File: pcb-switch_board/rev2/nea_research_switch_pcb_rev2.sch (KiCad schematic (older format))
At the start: 20 parts, among them P1 CONN_02X15, P2 CONN_02X13, P3 CONN_02X30, U1 QS4A110, U2 QS4A110, U3 QS4A110, U4 QS4A110, U5 QS4A110

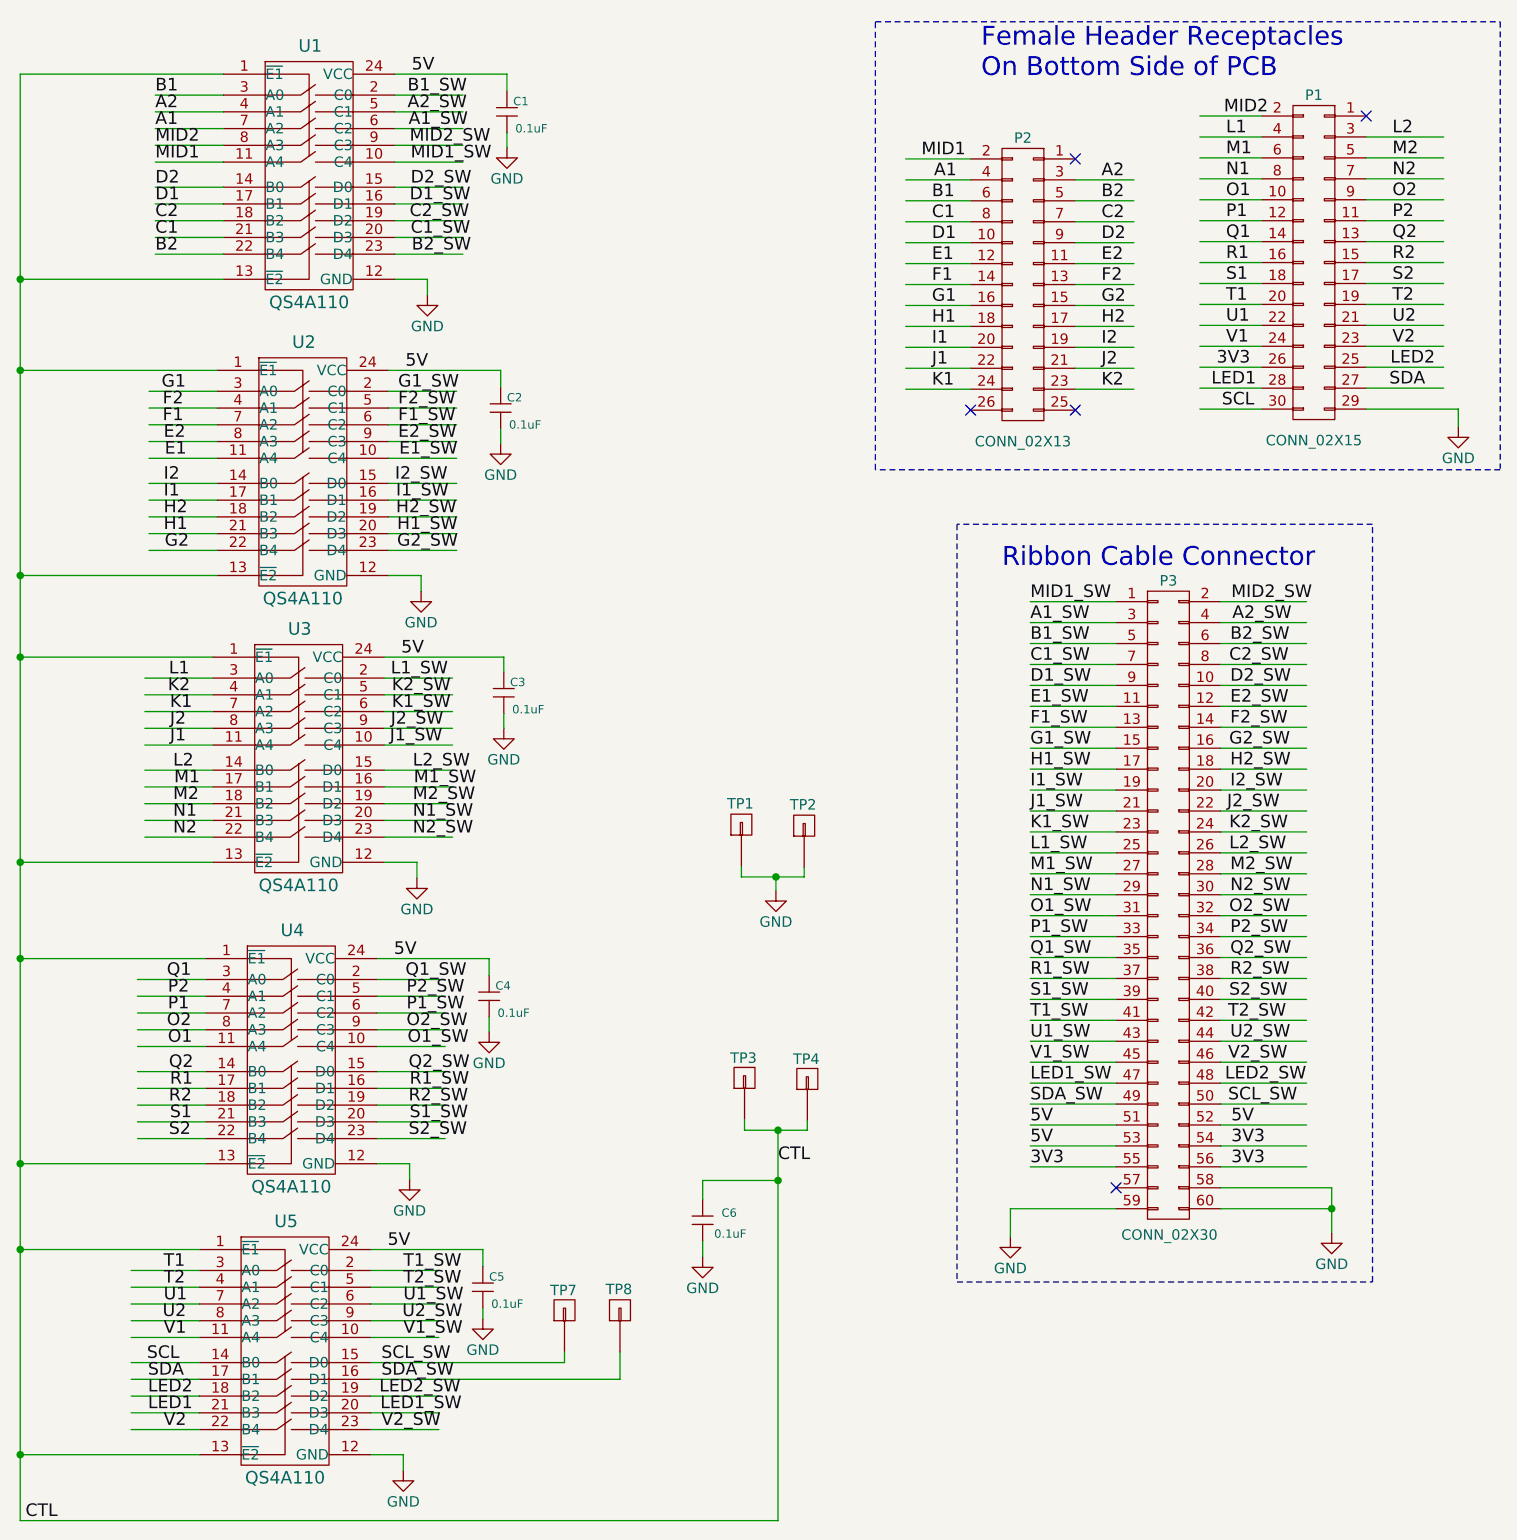
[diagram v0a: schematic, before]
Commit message: -revised breakout board to use BME280 sensor for SPI instead of I2C -revised switch board to accomodate SPI bus(2 extra signals) -added SPI bus testpoints to both boards -organized breakout and switch boards into rev1 and rev2 directories -gerbers for both boards created and this is what was ordered for rev2 boards
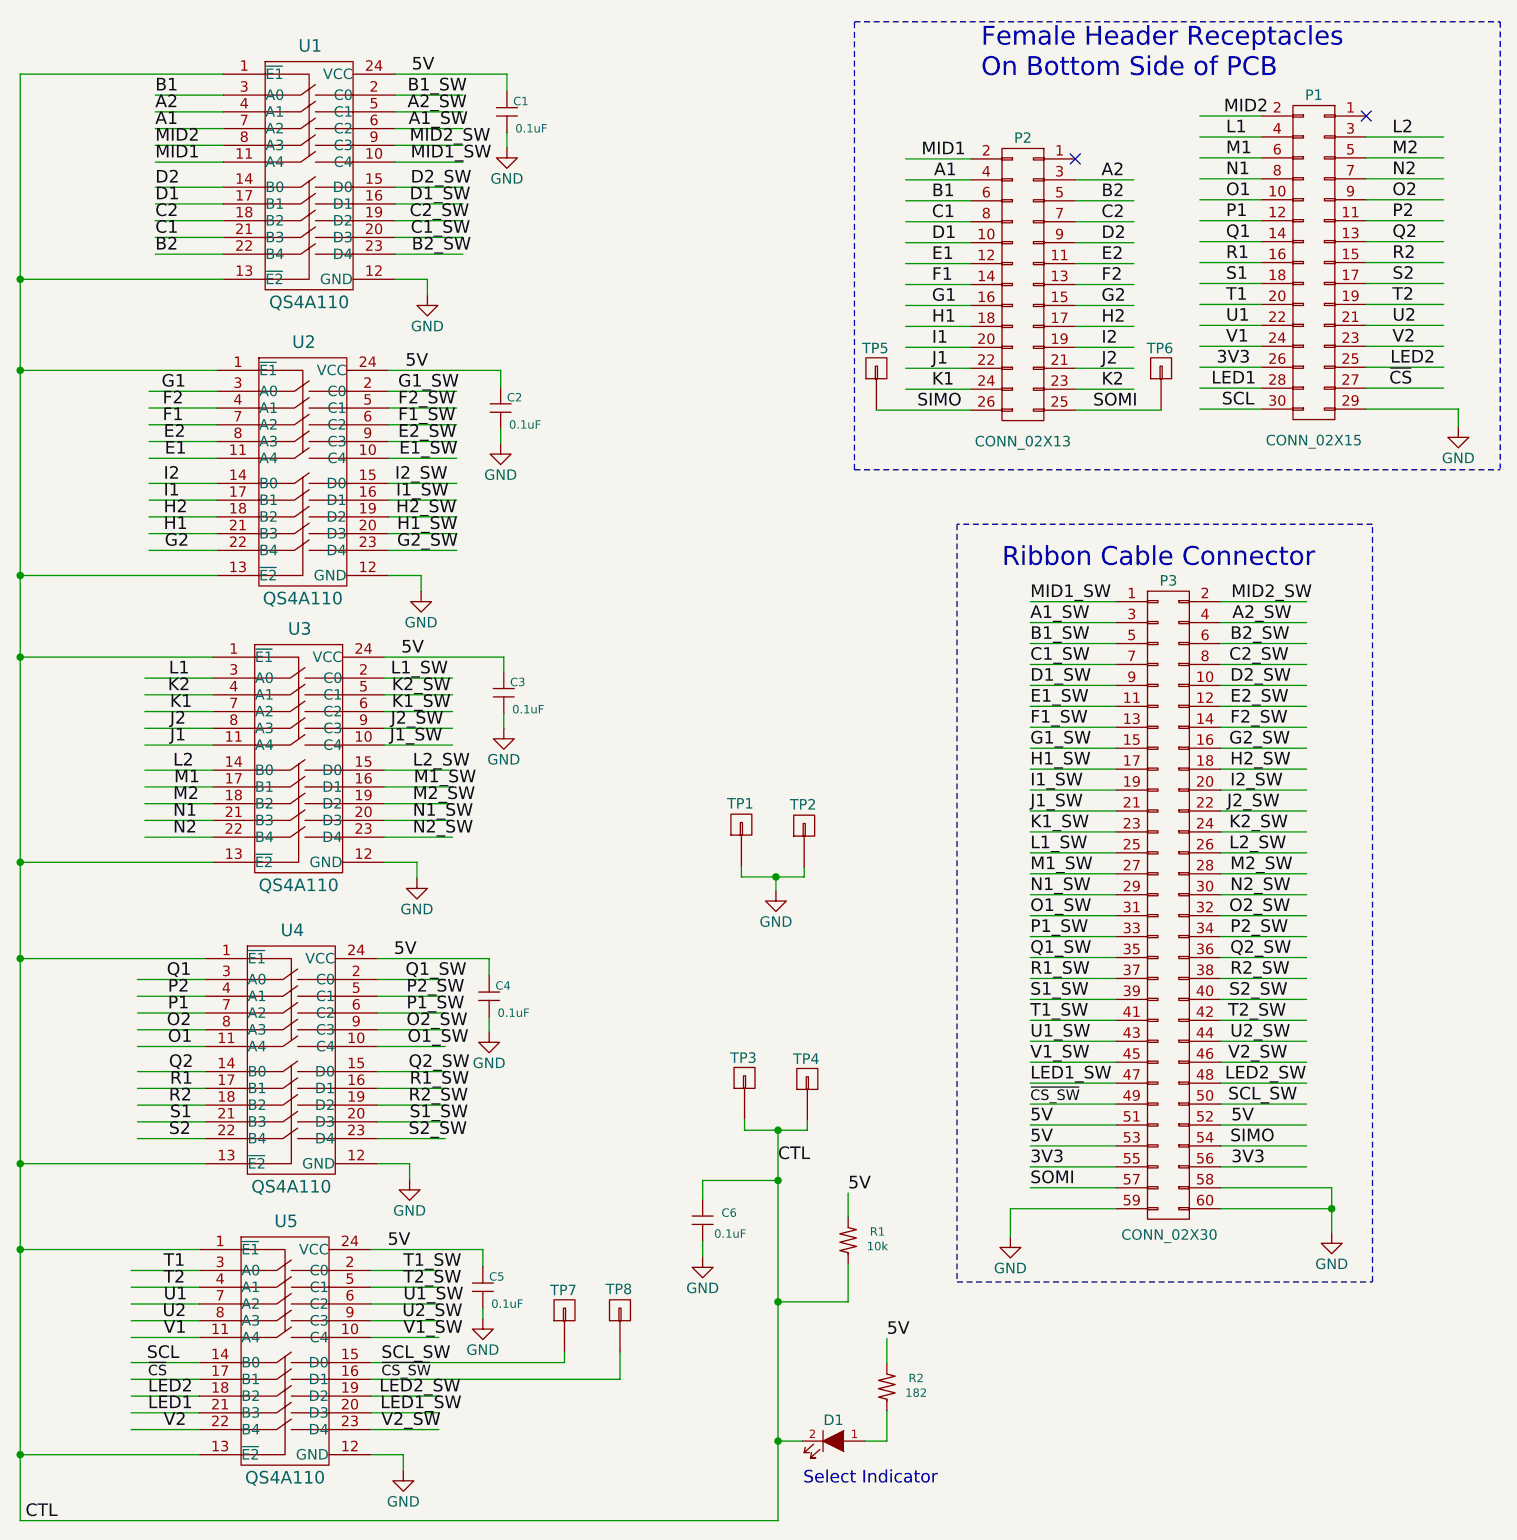
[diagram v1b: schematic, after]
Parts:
- added D1: LED_SMT, footprints:0603-D, symbol LED_SMT
- added R1: 10k, footprints_on_Cdrive:0603, symbol Res1_1
- added R2: 182, footprints_on_Cdrive:0603, symbol Res1_1
- added TP5, TP6: header_pin, footprints_on_Cdrive:Header_Pin_Rnd, symbol header_pin
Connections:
- net labels added: SIMO, SOMI, ~CS, ~CS_SW
- net labels removed: SDA, SDA_SW
- wire segments 264 -> 274
- no-connect marks 5 -> 2
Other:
- note added: "Select Indicator"
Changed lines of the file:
@@
 LIBS:valves
 LIBS:misc_parts
-LIBS:nea_research_pcb_rev1_switch-cache
+LIBS:nea_research_switch_pcb_rev2-cache
 EELAYER 25 0
 EELAYER END
@@
 Title "Schematic - NEA Research Fixture Switch PCB"
 Date "2017-02-09"
-Rev "1"
+Rev "2"
 Comp "Custom Silicon Solutions"
 Comment1 ""
@@
 SCL
 Text Label 7465 2395 0    60   ~ 0
-SDA
+~CS
 Text Label 6615 2395 0    60   ~ 0
 LED1
@@
 LED2
 $Comp
-L GND #PWR3
+L GND #PWR01
 U 1 1 588CBF4C
 P 7795 2580
-F 0 "#PWR3" H 7795 2330 50  0001 C CNN
+F 0 "#PWR01" H 7795 2330 50  0001 C CNN
 F 1 "GND" H 7795 2430 50  0000 C CNN
 F 2 "" H 7795 2580 50  0000 C CNN
@@
 	1    0    0    -1
 $EndComp
-NoConn ~ 5465 2500
-NoConn ~ 5965 2500
 Wire Wire Line
 	7795 2495 7795 2580
@@
 	6855 2395 6560 2395
 Wire Notes Line
-	7995 2785 5010 2785
+	4910 2785 7995 2785
 Wire Notes Line
-	5010 2785 5010 645
+	4910 2785 4910 645
 Wire Notes Line
-	5010 645  7995 645
+	4910 645  7995 645
 Wire Notes Line
 	7995 645  7995 2780
@@
 Text Label 1530 7050 0    60   ~ 0
 SCL
-Text Label 1535 7130 0    60   ~ 0
-SDA
+Text Label 1535 7130 0    50   ~ 0
+~CS
 Text Label 1535 7290 0    60   ~ 0
 LED1
@@
 Text Label 2650 7050 0    60   ~ 0
 SCL_SW
-Text Label 2650 7130 0    60   ~ 0
-SDA_SW
+Text Label 2650 7130 0    50   ~ 0
+~CS_SW
 Text Label 2645 7290 0    60   ~ 0
 LED1_SW
@@
 	3040 1075 2715 1075
 Wire Wire Line
-	925  7805 4545 7805
-Wire Wire Line
-	925  895  925  7805
+	4545 7805 925  7805
+Wire Wire Line
+	925  7805 925  895
 Wire Wire Line
 	925  895  1895 895
@@
 CTL
 $Comp
-L GND #PWR2
+L GND #PWR02
 U 1 1 589AF5DF
 P 2870 1950
-F 0 "#PWR2" H 2870 1700 50  0001 C CNN
+F 0 "#PWR02" H 2870 1700 50  0001 C CNN
 F 1 "GND" H 2870 1800 50  0000 C CNN
 F 2 "" H 2870 1950 50  0000 C CNN
@@
 	2870 1875 2870 1950
 $Comp
-L GND #PWR5
+L GND #PWR03
 U 1 1 589AF9D6
 P 2840 3365
-F 0 "#PWR5" H 2840 3115 50  0001 C CNN
+F 0 "#PWR03" H 2840 3115 50  0001 C CNN
 F 1 "GND" H 2840 3215 50  0000 C CNN
 F 2 "" H 2840 3365 50  0000 C CNN
@@
 	2840 3290 2840 3365
 $Comp
-L GND #PWR7
+L GND #PWR04
 U 1 1 589AFAF0
 P 2820 4735
-F 0 "#PWR7" H 2820 4485 50  0001 C CNN
+F 0 "#PWR04" H 2820 4485 50  0001 C CNN
 F 1 "GND" H 2820 4585 50  0000 C CNN
 F 2 "" H 2820 4735 50  0000 C CNN
@@
 	2820 4660 2820 4735
 $Comp
-L GND #PWR10
+L GND #PWR05
 U 1 1 589AFBFA
 P 2785 6175
-F 0 "#PWR10" H 2785 5925 50  0001 C CNN
+F 0 "#PWR05" H 2785 5925 50  0001 C CNN
 F 1 "GND" H 2785 6025 50  0000 C CNN
 F 2 "" H 2785 6175 50  0000 C CNN
@@
 	2785 6100 2785 6175
 $Comp
-L GND #PWR15
+L GND #PWR06
 U 1 1 589AFCD4
 P 2755 7565
-F 0 "#PWR15" H 2755 7315 50  0001 C CNN
+F 0 "#PWR06" H 2755 7315 50  0001 C CNN
 F 1 "GND" H 2755 7415 50  0000 C CNN
 F 2 "" H 2755 7565 50  0000 C CNN
@@
 Text Label 6695 5815 0    60   ~ 0
 SCL_SW
-Text Label 5750 5815 0    60   ~ 0
-SDA_SW
 Text Label 5750 5715 0    60   ~ 0
 LED1_SW
@@
 Text Label 5750 6015 0    60   ~ 0
 5V
-Text Label 6710 6015 0    60   ~ 0
-3V3
 Text Label 5750 6115 0    60   ~ 0
 3V3
+Text Label 6705 6015 0    60   ~ 0
+SIMO
 Text Label 6710 6115 0    60   ~ 0
 3V3
 $Comp
-L GND #PWR12
+L GND #PWR07
 U 1 1 589B55C6
 P 5655 6450
-F 0 "#PWR12" H 5655 6200 50  0001 C CNN
+F 0 "#PWR07" H 5655 6200 50  0001 C CNN
 F 1 "GND" H 5655 6300 50  0000 C CNN
 F 2 "" H 5655 6450 50  0000 C CNN
@@
 $EndComp
 $Comp
-L GND #PWR11
+L GND #PWR08
 U 1 1 589B55E9
 P 7190 6430
-F 0 "#PWR11" H 7190 6180 50  0001 C CNN
+F 0 "#PWR08" H 7190 6180 50  0001 C CNN
 F 1 "GND" H 7190 6280 50  0000 C CNN
 F 2 "" H 7190 6430 50  0000 C CNN
@@
 $EndComp
 $Comp
-L GND #PWR6
+L GND #PWR09
 U 1 1 589D14F4
 P 3235 4020
-F 0 "#PWR6" H 3235 3770 50  0001 C CNN
+F 0 "#PWR09" H 3235 3770 50  0001 C CNN
 F 1 "GND" H 3235 3870 50  0000 C CNN
 F 2 "" H 3235 4020 50  0000 C CNN
@@
 $EndComp
 $Comp
-L GND #PWR4
+L GND #PWR010
 U 1 1 589D1D03
 P 3220 2660
-F 0 "#PWR4" H 3220 2410 50  0001 C CNN
+F 0 "#PWR010" H 3220 2410 50  0001 C CNN
 F 1 "GND" H 3220 2510 50  0000 C CNN
 F 2 "" H 3220 2660 50  0000 C CNN
@@
 $EndComp
 $Comp
-L GND #PWR1
+L GND #PWR011
 U 1 1 589D2222
 P 3250 1245
-F 0 "#PWR1" H 3250 995 50  0001 C CNN
+F 0 "#PWR011" H 3250 995 50  0001 C CNN
 F 1 "GND" H 3250 1095 50  0000 C CNN
 F 2 "" H 3250 1245 50  0000 C CNN
@@
 $EndComp
 $Comp
-L GND #PWR9
+L GND #PWR012
 U 1 1 589D2525
 P 3165 5470
-F 0 "#PWR9" H 3165 5220 50  0001 C CNN
+F 0 "#PWR012" H 3165 5220 50  0001 C CNN
 F 1 "GND" H 3165 5320 50  0000 C CNN
 F 2 "" H 3165 5470 50  0000 C CNN
@@
 $EndComp
 $Comp
-L GND #PWR14
+L GND #PWR013
 U 1 1 589D26E0
 P 3135 6840
-F 0 "#PWR14" H 3135 6590 50  0001 C CNN
+F 0 "#PWR013" H 3135 6590 50  0001 C CNN
 F 1 "GND" H 3135 6690 50  0000 C CNN
 F 2 "" H 3135 6840 50  0000 C CNN
@@
 	3790 7130 3790 7000
 $Comp
-L GND #PWR8
+L GND #PWR014
 U 1 1 589D88A3
 P 4535 4795
-F 0 "#PWR8" H 4535 4545 50  0001 C CNN
+F 0 "#PWR014" H 4535 4545 50  0001 C CNN
 F 1 "GND" H 4535 4645 50  0000 C CNN
 F 2 "" H 4535 4795 50  0000 C CNN
@@
 Wire Wire Line
 	4685 5940 4685 5895
-NoConn ~ 6160 6215
-Wire Wire Line
-	4545 7805 4545 5940
+Wire Wire Line
+	4545 5940 4545 7805
 Connection ~ 4545 5940
 $Comp
@@
 $EndComp
 $Comp
-L GND #PWR13
+L GND #PWR015
 U 1 1 589E460E
 P 4185 6545
-F 0 "#PWR13" H 4185 6295 50  0001 C CNN
+F 0 "#PWR015" H 4185 6295 50  0001 C CNN
 F 1 "GND" H 4185 6395 50  0000 C CNN
 F 2 "" H 4185 6545 50  0000 C CNN
@@
 	4185 6180 4545 6180
 Connection ~ 4545 6180
+$Comp
+L Res1_1 R1
+U 1 1 589E9FC0
+P 4880 6455
+F 0 "R1" H 5020 6485 40  0000 C CNN
+F 1 "10k" H 5020 6415 40  0000 C CNN
+F 2 "footprints_on_Cdrive:0603" H 4935 6175 30  0001 C CNN
+F 3 "" H 4880 6455 30  0000 C CNN
+F 4 " RES SMD 10K OHM 1% 1/10W 0603 " H 5230 6085 60  0001 C CNN "description"
+F 5 "digikey" H 4670 5970 60  0001 C CNN "supplier"
+F 6 "311-10.0KHRCT-ND" H 5475 5955 60  0001 C CNN "supplier pn"
+F 7 "Yageo" H 4255 5845 60  0001 C CNN "manufacturer"
+F 8 "RC0603FR-0710KL " H 5355 5850 60  0001 C CNN "manufacturer pn"
+	1    4880 6455
+	1    0    0    -1
+$EndComp
+Wire Wire Line
+	4880 6355 4880 6240
+Wire Wire Line
+	4880 6580 4880 6760
+Text Label 4880 6240 0    60   ~ 0
+5V
+$Comp
+L LED_SMT D1
+U 1 1 589EBF8D
+P 4810 7425
+F 0 "D1" H 4810 7525 50  0000 C CNN
+F 1 "LED_SMT" H 4835 7275 50  0001 C CNN
+F 2 "footprints:0603-D" H 4860 8025 60  0001 C CNN
+F 3 "" H 4810 7425 60  0000 C CNN
+F 4 "LED 1.6X0.8MM 568NM GRN CLR SMD" H 4960 7725 50  0001 C CNN "description"
+F 5 "digikey" H 4585 7825 50  0001 C CNN "supplier"
+F 6 "754-1121-1-ND" H 5110 7825 50  0001 C CNN "supplier pn"
+F 7 "Kingbright" H 4560 7925 50  0001 C CNN "manufacturer"
+F 8 "APT1608SGC" H 5060 7925 50  0001 C CNN "manufacturer pn"
+	1    4810 7425
+	-1   0    0    -1
+$EndComp
+$Comp
+L Res1_1 R2
+U 1 1 589EC8D4
+P 5065 7155
+F 0 "R2" H 5205 7185 40  0000 C CNN
+F 1 "182" H 5205 7115 40  0000 C CNN
+F 2 "footprints_on_Cdrive:0603" H 5120 6875 30  0001 C CNN
+F 3 "" H 5065 7155 30  0000 C CNN
+F 4 "RES SMD 182 OHM 1% 1/10W 0603 " H 5415 6785 60  0001 C CNN "description"
+F 5 "digikey" H 4855 6670 60  0001 C CNN "supplier"
+F 6 " 311-182HRCT-ND " H 5660 6655 60  0001 C CNN "supplier pn"
+F 7 "Yageo" H 4440 6545 60  0001 C CNN "manufacturer"
+F 8 "RC0603FR-07182RL " H 5540 6550 60  0001 C CNN "manufacturer pn"
+	1    5065 7155
+	1    0    0    -1
+$EndComp
+Wire Wire Line
+	4880 6760 4545 6760
+Connection ~ 4545 6760
+Wire Wire Line
+	5065 7055 5065 6935
+Wire Wire Line
+	5065 7280 5065 7425
+Wire Wire Line
+	5065 7425 4960 7425
+Wire Wire Line
+	4660 7425 4545 7425
+Connection ~ 4545 7425
+Text Label 5065 6935 0    60   ~ 0
+5V
+Text Notes 4665 7640 0    60   ~ 0
+Select Indicator
+Text Label 6050 2500 0    60   ~ 0
+SOMI
+Wire Wire Line
+	5965 2500 6375 2500
+Text Label 5210 2500 0    60   ~ 0
+SIMO
+Wire Wire Line
+	5015 2500 5465 2500
+Text Label 5750 6215 0    60   ~ 0
+SOMI
+Wire Wire Line
+	5750 6215 6160 6215
+Text Label 5750 5815 0    50   ~ 0
+~CS_SW
+$Comp
+L header_pin TP5
+U 1 1 58A9074B
+P 5015 2300
+F 0 "TP5" V 5110 2305 50  0000 C CNN
+F 1 "header_pin" V 5115 2300 50  0001 C CNN
+F 2 "footprints_on_Cdrive:Header_Pin_Rnd" H 5015 2300 60  0001 C CNN
+F 3 "" H 5015 2300 60  0000 C CNN
+	1    5015 2300
+	0    -1   -1   0
+$EndComp
+$Comp
+L header_pin TP6
+U 1 1 58A91685
+P 6375 2300
+F 0 "TP6" V 6470 2305 50  0000 C CNN
+F 1 "header_pin" V 6475 2300 50  0001 C CNN
+F 2 "footprints_on_Cdrive:Header_Pin_Rnd" H 6375 2300 60  0001 C CNN
+F 3 "" H 6375 2300 60  0000 C CNN
+	1    6375 2300
+	0    -1   -1   0
+$EndComp
 $EndSCHEMATC

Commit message: -added BOM and files for measurement board assembly house
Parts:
- P1: manufacturer pn 2-146134-1 -> 1-534998-5; supplier pn A107235-ND -> A26494-ND
- P2: description CONN RECEPT 30POS .100 VERT DUAL -> CONN RECEPT 26POS .100 VERT DUAL; manufacturer pn 1-534998-5 -> 1-534998-3; supplier pn A26494-ND -> A26492-ND
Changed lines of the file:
@@
 F 3 "" H 7105 645 50  0000 C CNN
 F 4 "digikey" H 7105 1795 60  0001 C CNN "supplier"
-F 5 "A107235-ND " H 7105 1795 60  0001 C CNN "supplier pn"
+F 5 "A26494-ND " H 7105 1795 60  0001 C CNN "supplier pn"
 F 6 "TE" H 7105 1795 60  0001 C CNN "manufacturer"
-F 7 "2-146134-1 " H 7105 1795 60  0001 C CNN "manufacturer pn"
+F 7 "1-534998-5" H 7105 1795 60  0001 C CNN "manufacturer pn"
 F 8 "CONN HEADER B/A 30POS VERT DUAL SMT" H 7105 1795 60  0001 C CNN "description"
 	1    7105 1795
@@
 F 3 "" H 5715 750 50  0000 C CNN
 F 4 "digikey" H 5715 1900 60  0001 C CNN "supplier"
-F 5 "A26494-ND" H 5715 1900 60  0001 C CNN "supplier pn"
+F 5 "A26492-ND" H 5715 1900 60  0001 C CNN "supplier pn"
 F 6 "TE" H 5715 1900 60  0001 C CNN "manufacturer"
-F 7 "1-534998-5 " H 5715 1900 60  0001 C CNN "manufacturer pn"
-F 8 "CONN RECEPT 30POS .100 VERT DUAL " H 5715 1900 60  0001 C CNN "description"
+F 7 "1-534998-3 " H 5715 1900 60  0001 C CNN "manufacturer pn"
+F 8 "CONN RECEPT 26POS .100 VERT DUAL " H 5715 1900 60  0001 C CNN "description"
 	1    5715 1900
 	-1   0    0    -1
